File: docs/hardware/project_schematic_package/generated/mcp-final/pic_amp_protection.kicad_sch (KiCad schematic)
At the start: 7 parts, among them J3 LCD_I2C, J4 PTT_COMP_IF, J5 ENCODER, J6 TX_SEQ_TRIP, J7 SWR_SENSE, J8 ANALOG_SENSE, U1 MCU

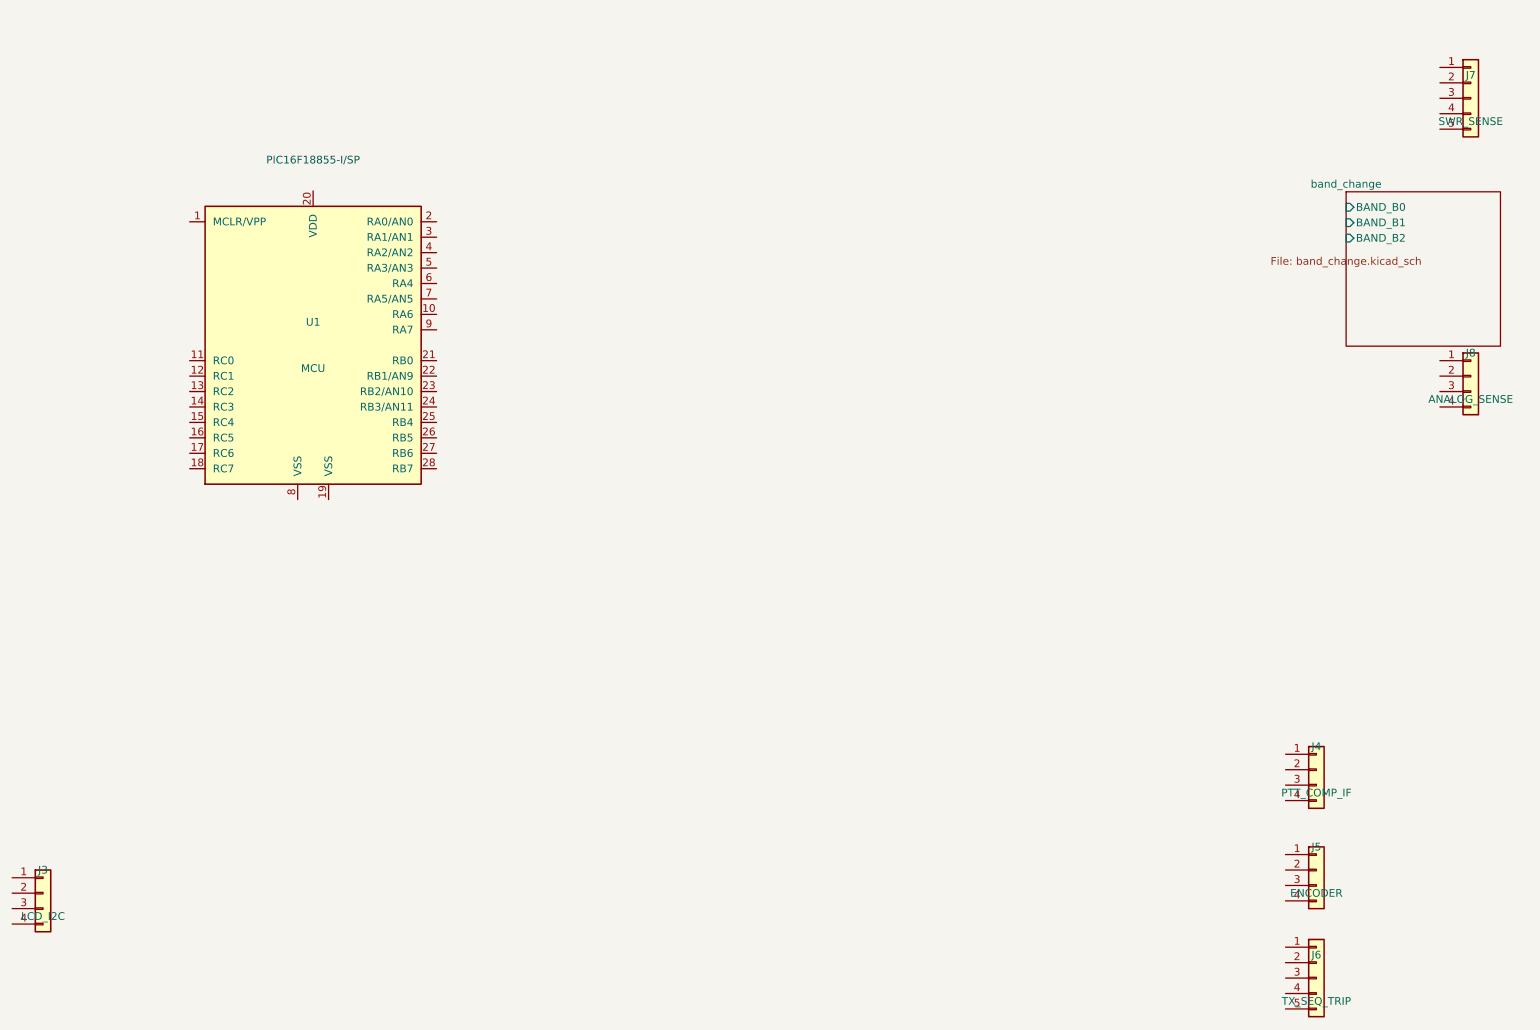
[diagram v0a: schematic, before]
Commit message: Enforce serialized KiCad writes and clean connector labels
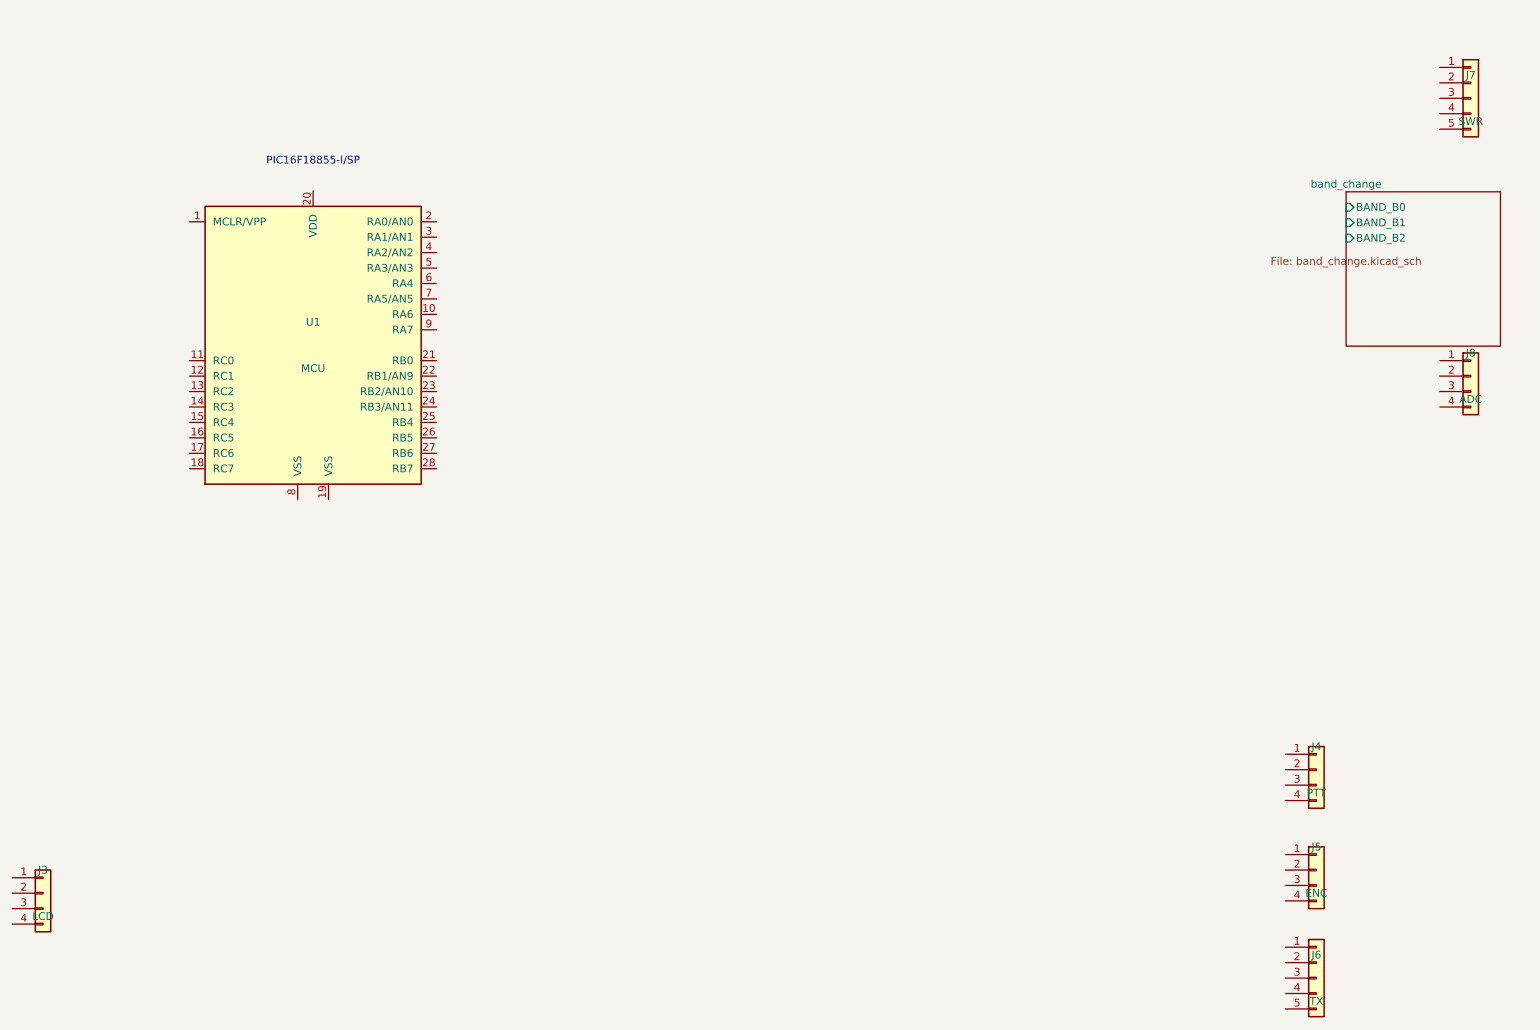
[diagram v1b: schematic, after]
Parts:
- J3: value LCD_I2C -> LCD
- J4: value PTT_COMP_IF -> PTT
- J5: value ENCODER -> ENC
- J6: value TX_SEQ_TRIP -> TX
- J7: value SWR_SENSE -> SWR
- J8: value ANALOG_SENSE -> ADC
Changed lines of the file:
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@@
 		)
 	)
-	(property "Value" "LCD_I2C"
+	(property "Value" "LCD"
 		(at 35.56 189.23 0)
 		(effects
@@
 		)
 	)
-	(property "Value" "PTT_COMP_IF"
+	(property "Value" "PTT"
 		(at 245.11 168.91 0)
 		(effects
@@
 		)
 	)
-	(property "Value" "ENCODER"
+	(property "Value" "ENC"
 		(at 245.11 185.42 0)
 		(effects
@@
 		)
 	)
-	(property "Value" "TX_SEQ_TRIP"
+	(property "Value" "TX"
 		(at 245.11 203.2 0)
 		(effects
@@
 		)
 	)
-	(property "Value" "SWR_SENSE"
+	(property "Value" "SWR"
 		(at 270.51 58.42 0)
 		(effects
@@
 		)
 	)
-	(property "Value" "ANALOG_SENSE"
+	(property "Value" "ADC"
 		(at 270.51 104.14 0)
 		(effects
@@
 			(reference "J3")
 			(unit 1)
-			(value "LCD_I2C")
+			(value "LCD")
 			(footprint "")
 		)
@@
 			(reference "J4")
 			(unit 1)
-			(value "PTT_COMP_IF")
+			(value "PTT")
 			(footprint "")
 		)
@@
 			(reference "J5")
 			(unit 1)
-			(value "ENCODER")
+			(value "ENC")
 			(footprint "")
 		)
@@
 			(reference "J6")
 			(unit 1)
-			(value "TX_SEQ_TRIP")
+			(value "TX")
 			(footprint "")
 		)
@@
 			(reference "J7")
 			(unit 1)
-			(value "SWR_SENSE")
+			(value "SWR")
 			(footprint "")
 		)
@@
 			(reference "J8")
 			(unit 1)
-			(value "ANALOG_SENSE")
-			(footprint "")
-		)
+			(value "ADC")
+			(footprint "")
+		)

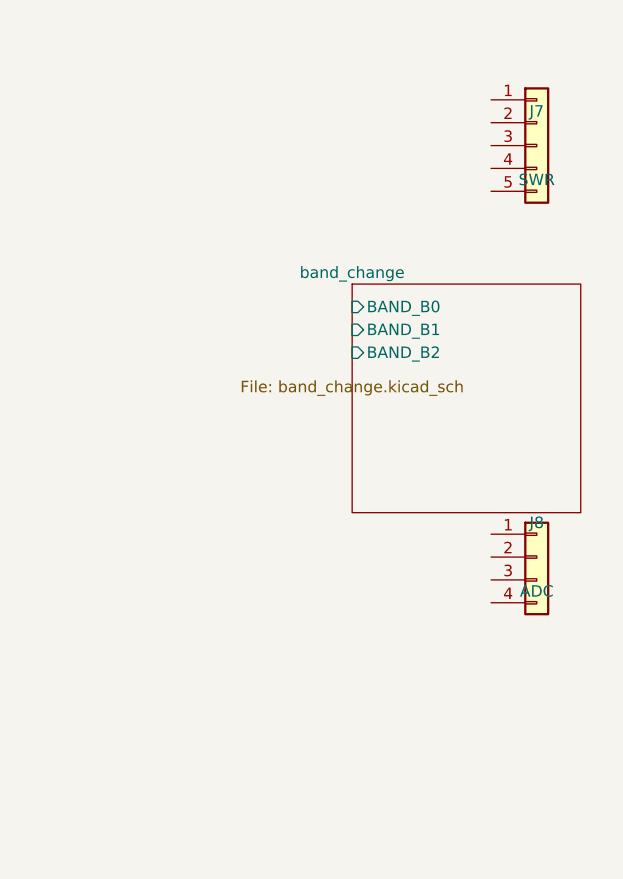
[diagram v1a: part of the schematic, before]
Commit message: Eliminate hierarchy and connector text overlaps
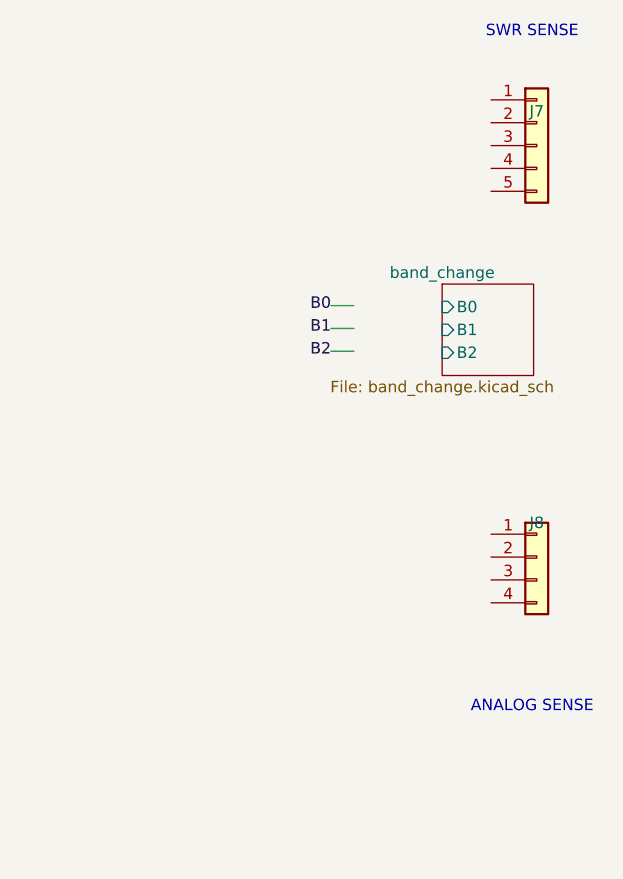
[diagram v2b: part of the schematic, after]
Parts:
- J7: value SWR -> (none)
- J8: value ADC -> (none)
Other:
- sheet band_change ports: added B0, B1, B2; removed BAND_B0, BAND_B1, BAND_B2
- note added: "ANALOG SENSE"
- note added: "SWR SENSE"
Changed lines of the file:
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@@
 		)
 	)
-	(property "Value" "SWR"
+	(property "Value" ""
 		(at 270.51 58.42 0)
 		(effects
@@
 		)
 	)
-	(property "Value" "ADC"
+	(property "Value" ""
 		(at 270.51 104.14 0)
 		(effects
@@
 			(reference "J7")
 			(unit 1)
-			(value "SWR")
+			(value "")
 			(footprint "")
 		)
@@
 			(reference "J8")
 			(unit 1)
-			(value "ADC")
+			(value "")
 			(footprint "")
 		)
@@
 			(footprint "")
 		)
+		(path "/5f892659-1480-447d-b5a7-bee1c920df64/31fdadf7-a534-4a85-9ba3-495bc9e15ecd/315bfe58-d863-4a17-bb4f-cd7295c6dde2"
+			(reference "U2")
+			(unit 1)
+			(value "74HC4514")
+			(footprint "")
+		)
+		(path "/5f892659-1480-447d-b5a7-bee1c920df64/31fdadf7-a534-4a85-9ba3-495bc9e15ecd/3f4089c8-3162-4b11-ae04-58b8143b1803"
+			(reference "U3")
+			(unit 1)
+			(value "ULN2803A")
+			(footprint "")
+		)
 )
 	(text "PIC16F18855-I/SP"
@@
 	)
 )
+	(text "SWR SENSE"
+	(at 270 42 0)
+	(effects
+		(font
+			(size 1.27 1.27)
+		)
+	)
+)
+	(text "ANALOG SENSE"
+	(at 270 117 0)
+	(effects
+		(font
+			(size 1.27 1.27)
+		)
+	)
+)
+	(wire
+	(pts
+		(xy 250.19 72.39) (xy 247.65 72.39)
+	)
+	(stroke
+		(width 0)
+		(type default)
+	)
+)
+	(wire
+	(pts
+		(xy 250.19 74.93) (xy 247.65 74.93)
+	)
+	(stroke
+		(width 0)
+		(type default)
+	)
+)
+	(wire
+	(pts
+		(xy 250.19 77.47) (xy 247.65 77.47)
+	)
+	(stroke
+		(width 0)
+		(type default)
+	)
+)
+	(label "B0"
+	(at 247.65 72.39 180)
+	(effects
+		(font
+			(size 1.27 1.27)
+		)
+	)
+)
+	(label "B1"
+	(at 247.65 74.93 180)
+	(effects
+		(font
+			(size 1.27 1.27)
+		)
+	)
+)
+	(label "B2"
+	(at 247.65 77.47 180)
+	(effects
+		(font
+			(size 1.27 1.27)
+		)
+	)
+)
 	(sheet
-	(at 250 70)
-	(size 25.4 25.4)
+	(at 260 70)
+	(size 10.16 10.16)
 	(fields_autoplaced yes)
 	(stroke
@@
 	)
 	(property "Sheetname" "band_change"
-		(at 250 68.73 0)
+		(at 260 68.73 0)
 		(effects
 			(font
@@
 	)
 	(property "Sheetfile" "band_change.kicad_sch"
-		(at 250 81.43 0)
-		(effects
-			(font
-				(size 1.27 1.27)
-			)
-		)
-	)
-	(pin "BAND_B0" input
-	(at 250 72.54 180)
-	(effects
-		(font
-			(size 1.27 1.27)
-		)
-	)
-)
-	(pin "BAND_B1" input
-	(at 250 75.08 180)
-	(effects
-		(font
-			(size 1.27 1.27)
-		)
-	)
-)
-	(pin "BAND_B2" input
-	(at 250 77.62 180)
+		(at 260 81.43 0)
+		(effects
+			(font
+				(size 1.27 1.27)
+			)
+		)
+	)
+	(pin "B0" input
+	(at 260 72.54 180)
+	(effects
+		(font
+			(size 1.27 1.27)
+		)
+	)
+)
+	(pin "B1" input
+	(at 260 75.08 180)
+	(effects
+		(font
+			(size 1.27 1.27)
+		)
+	)
+)
+	(pin "B2" input
+	(at 260 77.62 180)
 	(effects
 		(font
@@
 	(instances
 		(project "pic_amp_protection"
-			(path "/5f892659-1480-447d-b5a7-bee1c920df64/66194545-7c0e-4ce0-a254-d0c89aad8641"
+			(path "/5f892659-1480-447d-b5a7-bee1c920df64/31fdadf7-a534-4a85-9ba3-495bc9e15ecd"
 				(page "2")
 			)

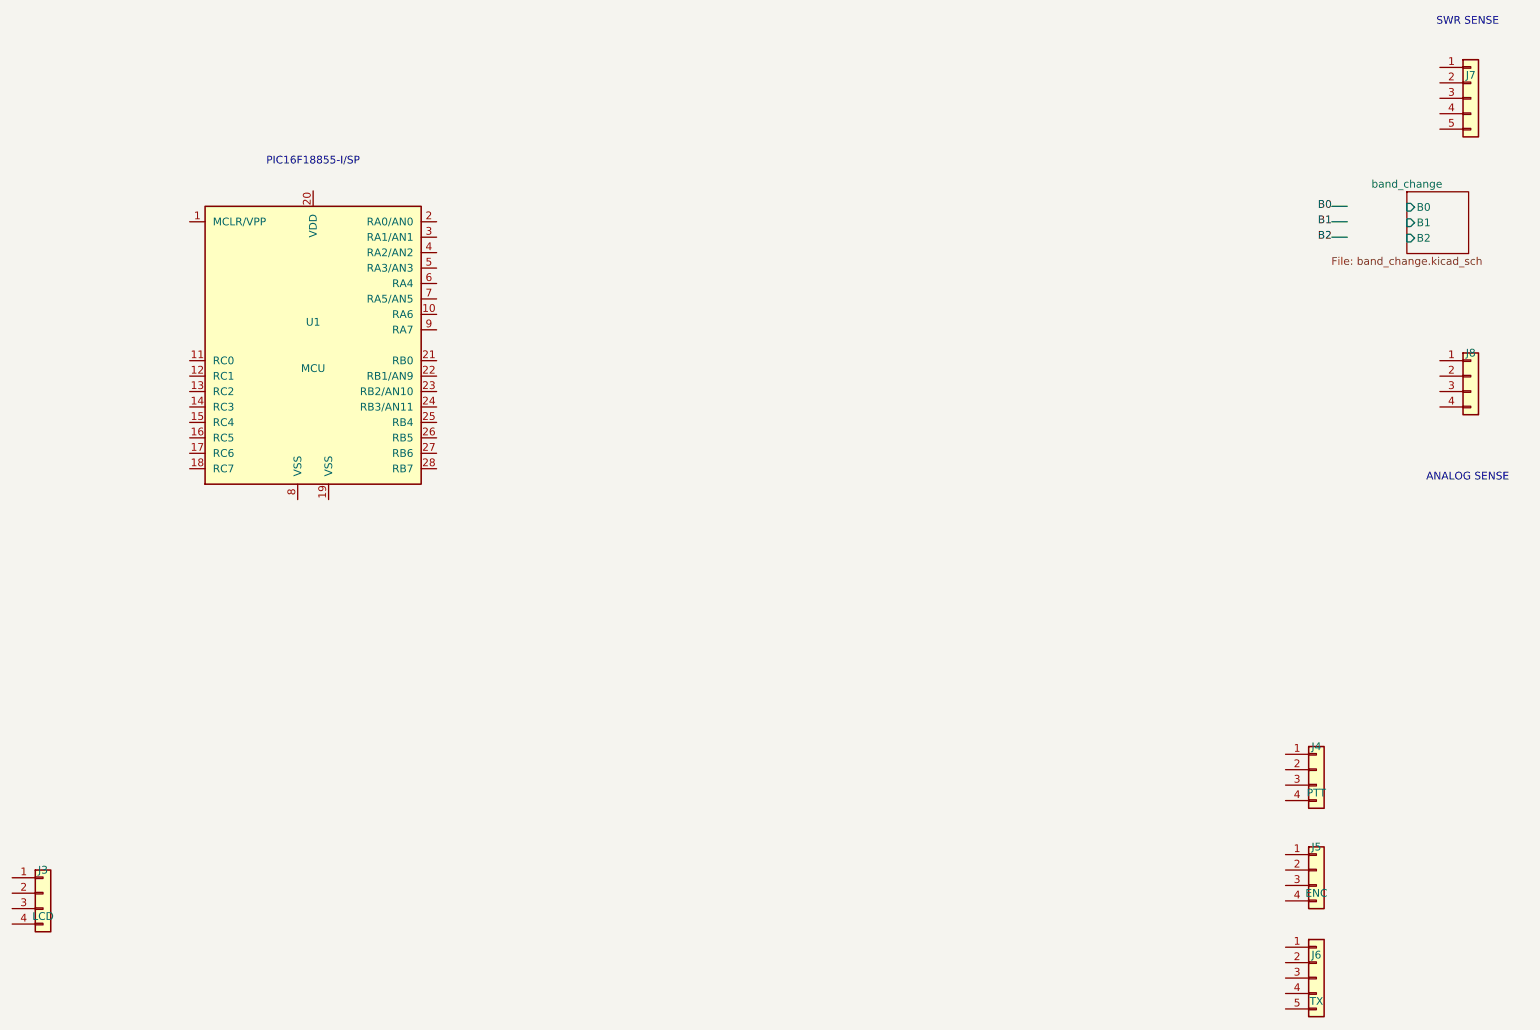
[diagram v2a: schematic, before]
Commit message: Move connector designations clear of pin fields
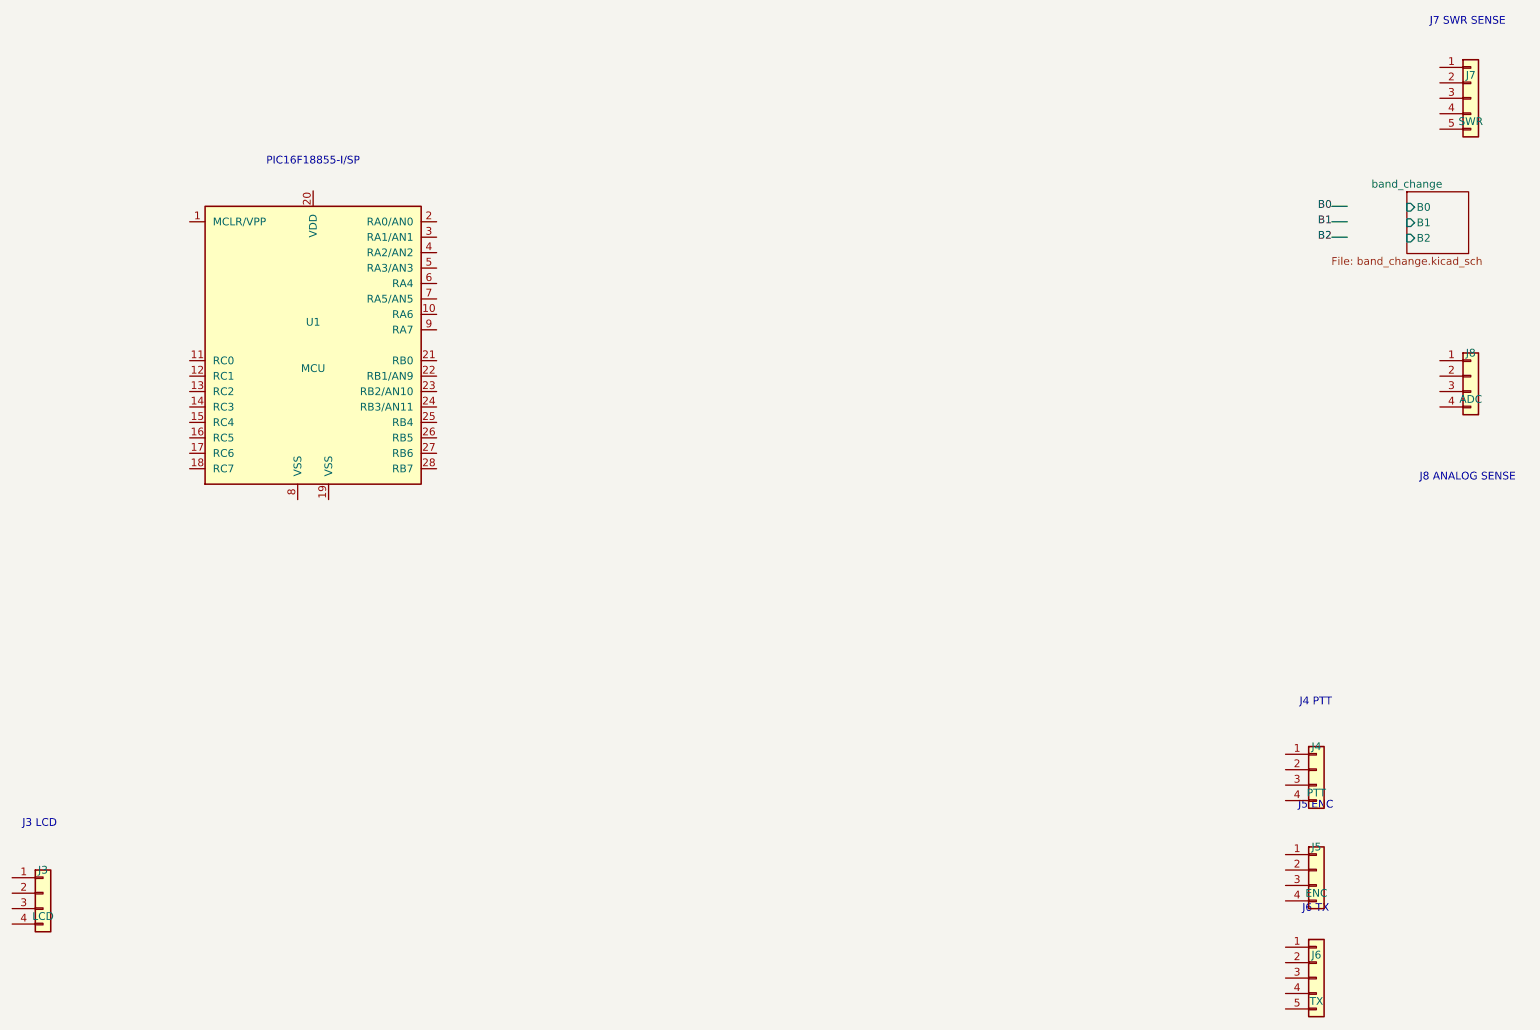
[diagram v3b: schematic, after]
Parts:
- J7: value (none) -> SWR
- J8: value (none) -> ADC
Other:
- note added: "J3 LCD"
- note added: "J4 PTT"
- note added: "J5 ENC"
- note added: "J6 TX"
- note added: "J7 SWR SENSE"
- note added: "J8 ANALOG SENSE"
- note removed: "ANALOG SENSE"
- note removed: "SWR SENSE"
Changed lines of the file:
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@@
 		)
 	)
-	(property "Value" ""
+	(property "Value" "SWR"
 		(at 270.51 58.42 0)
 		(effects
@@
 		)
 	)
-	(property "Value" ""
+	(property "Value" "ADC"
 		(at 270.51 104.14 0)
 		(effects
@@
 			(reference "J7")
 			(unit 1)
-			(value "")
+			(value "SWR")
 			(footprint "")
 		)
@@
 			(reference "J8")
 			(unit 1)
-			(value "")
+			(value "ADC")
 			(footprint "")
 		)
@@
 	)
 )
-	(text "SWR SENSE"
+	(text "J3 LCD"
+	(at 35 174 0)
+	(effects
+		(font
+			(size 1.27 1.27)
+		)
+	)
+)
+	(text "J4 PTT"
+	(at 245 154 0)
+	(effects
+		(font
+			(size 1.27 1.27)
+		)
+	)
+)
+	(text "J5 ENC"
+	(at 245 171 0)
+	(effects
+		(font
+			(size 1.27 1.27)
+		)
+	)
+)
+	(text "J6 TX"
+	(at 245 188 0)
+	(effects
+		(font
+			(size 1.27 1.27)
+		)
+	)
+)
+	(text "J7 SWR SENSE"
 	(at 270 42 0)
 	(effects
@@
 	)
 )
-	(text "ANALOG SENSE"
+	(text "J8 ANALOG SENSE"
 	(at 270 117 0)
 	(effects
